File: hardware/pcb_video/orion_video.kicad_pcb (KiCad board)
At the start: 4 copper layers, 99.7 x 99.7 mm, 0 parts

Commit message: Обновлена схема видеомодуля
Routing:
- removed copper zone on In1.Cu, net GND
- removed copper zone on In2.Cu, net VCC
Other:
- copper layers 4 -> 2

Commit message: Предварительное размещение элементов
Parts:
- added C1: 0.1u, Capacitors_SMD:C_0805, B.Cu at (190.5, 29.8)
- added C10: 0.1u, Capacitors_SMD:C_0805, F.Cu at (186.7, 132.7)
- added C11: 0.1u, Capacitors_SMD:C_0805, F.Cu at (190.5, 132.7)
- added C12: 0.1u, Capacitors_SMD:C_0805, F.Cu at (194.3, 132.7)
- added C13: 0.1u, Capacitors_SMD:C_0805, F.Cu at (198.1, 132.7)
- added C14: 0.1u, Capacitors_SMD:C_0805, F.Cu at (201.9, 132.7)
- added C15: 0.1u, Capacitors_SMD:C_0805, F.Cu at (171.4, 135.9)
- added C16: 0.1u, Capacitors_SMD:C_0805, F.Cu at (175.3, 135.9)
- added C17: 0.1u, Capacitors_SMD:C_0805, F.Cu at (179.1, 135.9)
- added C18: 0.1u, Capacitors_SMD:C_0805, F.Cu at (182.9, 135.9)
- added C19: 0.1u, Capacitors_SMD:C_0805, F.Cu at (186.7, 135.9)
- added C2: 10u, Capacitors_Tantalum_SMD:CP_Tantalum_Case-B_EIA-3528-21_Hand, F.Cu at (175.9, 127.6)
- added C20: 0.1u, Capacitors_SMD:C_0805, F.Cu at (190.5, 135.9)
- added C21: 0.1u, Capacitors_SMD:C_0805, F.Cu at (194.3, 135.9)
- added C22: 0.1u, Capacitors_SMD:C_0805, F.Cu at (198.1, 135.9)
- added C23: 0.1u, Capacitors_SMD:C_0805, F.Cu at (201.9, 135.9)
- added C24: 0.1u, Capacitors_SMD:C_0805, F.Cu at (171.4, 139.1)
- added C25: 0.1u, Capacitors_SMD:C_0805, F.Cu at (175.3, 139.1)
- added C26: 0.1u, Capacitors_SMD:C_0805, F.Cu at (179.1, 139.1)
- added C27: 0.1u, Capacitors_SMD:C_0805, F.Cu at (182.9, 139.1)
- added C28: 0.1u, Capacitors_SMD:C_0805, F.Cu at (186.7, 139.1)
- added C29: 0.1u, Capacitors_SMD:C_0805, F.Cu at (190.5, 139.1)
- added C3: 10u, Capacitors_Tantalum_SMD:CP_Tantalum_Case-B_EIA-3528-21_Hand, F.Cu at (184.5, 127.6)
- added C30: 0.1u, Capacitors_SMD:C_0805, F.Cu at (194.3, 139.1)
- added C31: 0.1u, Capacitors_SMD:C_0805, F.Cu at (198.1, 139.1)
- added C4: 10u, Capacitors_Tantalum_SMD:CP_Tantalum_Case-B_EIA-3528-21_Hand, F.Cu at (192.8, 127.6)
- added C5: 10u, Capacitors_Tantalum_SMD:CP_Tantalum_Case-B_EIA-3528-21_Hand, F.Cu at (201.1, 127.6)
- added C6: 0.1u, Capacitors_SMD:C_0805, F.Cu at (171.4, 132.7)
- added C7: 0.1u, Capacitors_SMD:C_0805, F.Cu at (175.3, 132.7)
- added C8: 0.1u, Capacitors_SMD:C_0805, F.Cu at (179.1, 132.7)
- added C9: 0.1u, Capacitors_SMD:C_0805, F.Cu at (182.9, 132.7)
- added DD1: IE18, Housings_SOIC:SOIC-16_3.9x9.9mm_Pitch1.27mm, F.Cu at (155.6, 64.1)
- added DD10: IR35, Housings_SOIC:SOIC-20W_7.5x12.8mm_Pitch1.27mm, F.Cu at (186.1, 104.1)
- added DD11: IR23, Housings_SOIC:SOIC-20W_7.5x12.8mm_Pitch1.27mm, F.Cu at (186.1, 89.5)
- added DD12: IR22, Housings_SOIC:SOIC-20W_7.5x12.8mm_Pitch1.27mm, F.Cu at (109.2, 61.6)
- added DD13: IR22, Housings_SOIC:SOIC-20W_7.5x12.8mm_Pitch1.27mm, F.Cu at (108.6, 76.2)
- added DD14: IR22, Housings_SOIC:SOIC-20W_7.5x12.8mm_Pitch1.27mm, F.Cu at (123.8, 76.2)
- added DD15: IR22, Housings_SOIC:SOIC-20W_7.5x12.8mm_Pitch1.27mm, B.Cu at (108.6, 76.2)
- added DD16: IR22, Housings_SOIC:SOIC-20W_7.5x12.8mm_Pitch1.27mm, B.Cu at (123.8, 76.2)
- added DD17: KP11, Housings_SOIC:SOIC-16_3.9x9.9mm_Pitch1.27mm, F.Cu at (125.7, 62.2)
- added DD18: 28C256, Sockets:PLCC44, F.Cu at (120.0, 42.5)
- added DD19: IR10, Housings_SOIC:SOIC-16_3.9x9.9mm_Pitch1.27mm, F.Cu at (141.6, 34.9)
- added DD2: IE18, Housings_SOIC:SOIC-16_3.9x9.9mm_Pitch1.27mm, F.Cu at (146.1, 64.1)
- added DD20: IR10, Housings_SOIC:SOIC-16_3.9x9.9mm_Pitch1.27mm, F.Cu at (155.6, 34.9)
- added DD21: IR10, Housings_SOIC:SOIC-16_3.9x9.9mm_Pitch1.27mm, F.Cu at (141.6, 47.6)
- added DD22: IR10, Housings_SOIC:SOIC-16_3.9x9.9mm_Pitch1.27mm, F.Cu at (155.6, 47.6)
- added DD23: ATF22V10, Housings_DIP:DIP-24_W7.62mm_Socket_LongPads, F.Cu at (167.6, 52.7)
- added DD24: KP11, Housings_SOIC:SOIC-16_3.9x9.9mm_Pitch1.27mm, F.Cu at (158.8, 87.6)
- added DD25: KP11, Housings_SOIC:SOIC-16_3.9x9.9mm_Pitch1.27mm, B.Cu at (158.8, 91.4)
- added DD26: KP11, Housings_SOIC:SOIC-16_3.9x9.9mm_Pitch1.27mm, F.Cu at (158.8, 97.2)
- added DD27: KP11, Housings_SOIC:SOIC-16_3.9x9.9mm_Pitch1.27mm, B.Cu at (158.8, 101.0)
- added DD28: ATF22V10, Housings_DIP:DIP-24_W7.62mm_Socket_LongPads, F.Cu at (139.7, 88.3)
- added DD29: AP6, Housings_SOIC:SOIC-20W_7.5x12.8mm_Pitch1.27mm, F.Cu at (120.0, 106.0)
- added DD3: IE18, Housings_SOIC:SOIC-16_3.9x9.9mm_Pitch1.27mm, F.Cu at (136.5, 64.1)
- added DD30: AP6, Housings_SOIC:SOIC-20W_7.5x12.8mm_Pitch1.27mm, B.Cu at (120.0, 106.0)
- added DD31, DD32: CY7C1049B, andreil:SOJ-36, F.Cu at (148.9, 132.0)
- added DD4: IE18, Housings_SOIC:SOIC-16_3.9x9.9mm_Pitch1.27mm, F.Cu at (174.6, 64.1)
- added DD5: IE18, Housings_SOIC:SOIC-16_3.9x9.9mm_Pitch1.27mm, F.Cu at (184.2, 64.1)
- added DD6: IE18, Housings_SOIC:SOIC-16_3.9x9.9mm_Pitch1.27mm, F.Cu at (193.7, 64.1)
- added DD7: ATF22V10, Housings_DIP:DIP-24_W7.62mm_Socket_LongPads, F.Cu at (161.9, 73.0)
- added DD8: ATF22V10, Housings_DIP:DIP-24_W7.62mm_Socket_LongPads, F.Cu at (195.6, 73.0)
- added DD9: IR35, Housings_SOIC:SOIC-20W_7.5x12.8mm_Pitch1.27mm, F.Cu at (136.5, 106.0)
- added J1: VGA, w_conn_pc:DB_15F-VGA, F.Cu at (182.0, 23.6)
- added J2: SYS_PRO, Socket_Strips:Socket_Strip_Straight_2x32_Pitch2.54mm, F.Cu at (109.9, 114.9)
- added J3: SYS_EXT, Socket_Strips:Socket_Strip_Straight_2x18_Pitch2.54mm, F.Cu at (109.2, 25.4)
- added J4: MEM1, Socket_Strips:Socket_Strip_Straight_2x12_Pitch2.00mm, F.Cu at (149.3, 85.9)
- added J5: MEM2, Socket_Strips:Socket_Strip_Straight_2x12_Pitch2.00mm, F.Cu at (105.4, 85.9)
- added JP1: 4:3, Socket_Strips:Socket_Strip_Straight_1x02_Pitch2.54mm, F.Cu at (169.5, 85.1)
- added JP2: GDS, Socket_Strips:Socket_Strip_Straight_2x08_Pitch2.54mm, F.Cu at (105.4, 34.3)
- added R1: 1k, Resistors_SMD:R_0805, F.Cu at (156.2, 128.9)
- added R10: 470, Resistors_SMD:R_0805, F.Cu at (177.8, 34.9)
- added R11: 470, Resistors_SMD:R_0805, F.Cu at (181.6, 40.0)
- added R12: 470, Resistors_SMD:R_0805, F.Cu at (181.6, 34.9)
- added R13: 1k, Resistors_SMD:R_0805, F.Cu at (175.3, 37.5)
- added R14: 1k, Resistors_SMD:R_0805, F.Cu at (179.1, 37.5)
- added R15: 1k, Resistors_SMD:R_0805, F.Cu at (182.9, 37.5)
- added R16: 510, Resistors_SMD:R_0805, F.Cu at (175.9, 33.7)
- added R17: 510, Resistors_SMD:R_0805, F.Cu at (179.7, 33.7)
- added R18: 510, Resistors_SMD:R_0805, F.Cu at (183.5, 33.7)
- added R19: 47, Resistors_SMD:R_0805, B.Cu at (181.6, 33.7)
- added R2: 1k, Resistors_SMD:R_0805, F.Cu at (159.4, 128.9)
- added R20: 47, Resistors_SMD:R_0805, B.Cu at (185.4, 33.7)
- added R3: 1k, Resistors_SMD:R_0805, F.Cu at (162.6, 128.9)
- added R4: 1k, Resistors_SMD:R_0805, F.Cu at (165.7, 128.9)
- added R5: 1k, Resistors_SMD:R_0805, F.Cu at (156.2, 132.0)
- added R6: 1k, Resistors_SMD:R_0805, F.Cu at (159.4, 132.1)
- added R7: 470, Resistors_SMD:R_0805, F.Cu at (174.0, 40.0)
- added R8: 470, Resistors_SMD:R_0805, F.Cu at (174.0, 34.9)
- added R9: 470, Resistors_SMD:R_0805, F.Cu at (177.8, 40.0)
- added REF**: MountingHole_3.2mm_M3_Pad, Mounting_Holes:MountingHole_3.2mm_M3_Pad, F.Cu at (194.3, 116.2)
- added REF**: MountingHole_3.2mm_M3_Pad, Mounting_Holes:MountingHole_3.2mm_M3_Pad, F.Cu at (103.5, 116.2)
- added REF**: MountingHole_3.2mm_M3_Pad, Mounting_Holes:MountingHole_3.2mm_M3_Pad, F.Cu at (103.5, 27.3)
- added REF**: MountingHole_3.2mm_M3_Pad, Mounting_Holes:MountingHole_3.2mm_M3_Pad, F.Cu at (193.7, 36.8)
- added U1, U2: AS7C4098A, andreil:SOJ-44, F.Cu at (148.9, 132.0)
- added Y1: 25MHz, Crystals:Crystal_SMD_7050-4pin_7.0x5.0mm, F.Cu at (165.1, 65.4)

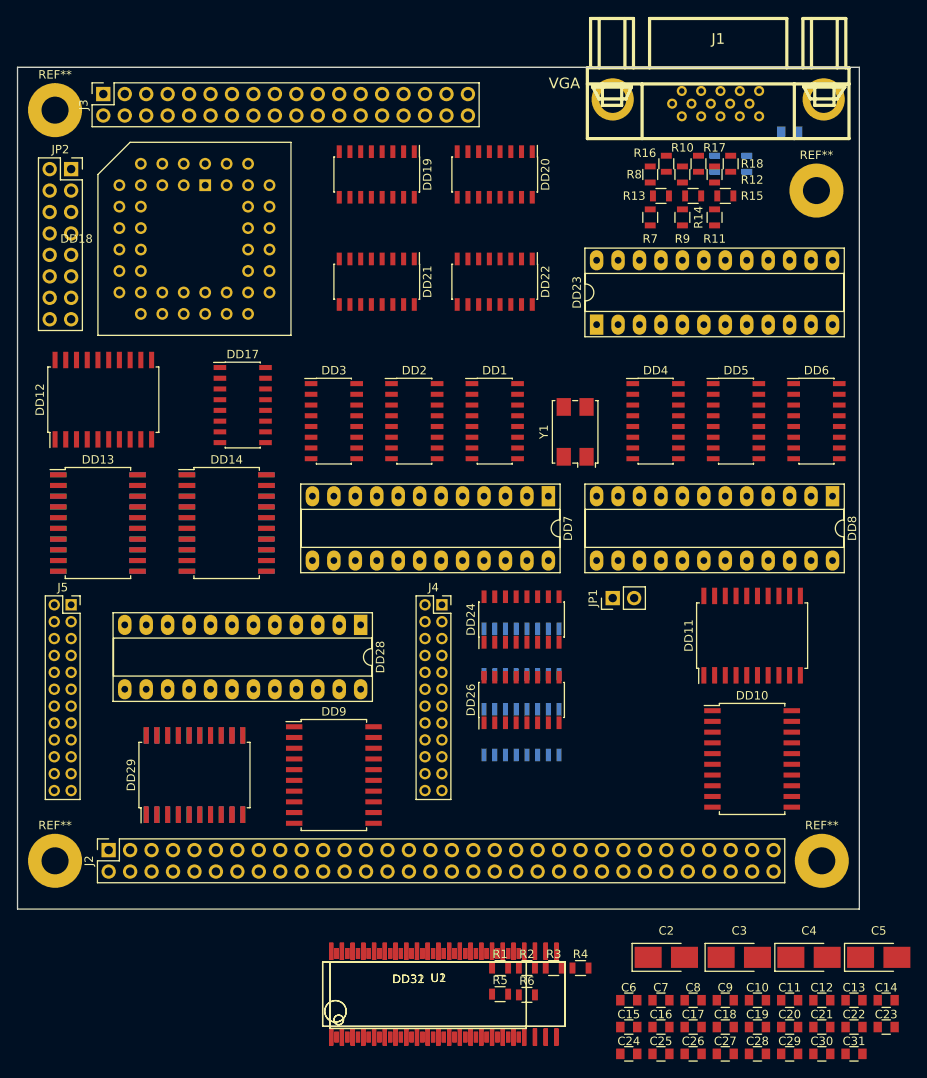
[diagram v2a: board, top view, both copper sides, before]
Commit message: Исправления по схеме видеомодуля:
1) Заменён системный разъём на DIN 41612;
2) ПЗУ знакогенератора заменена на 28C512;
3) Добавлена коммутация подачи питания на пин 9 разъёма VGA.
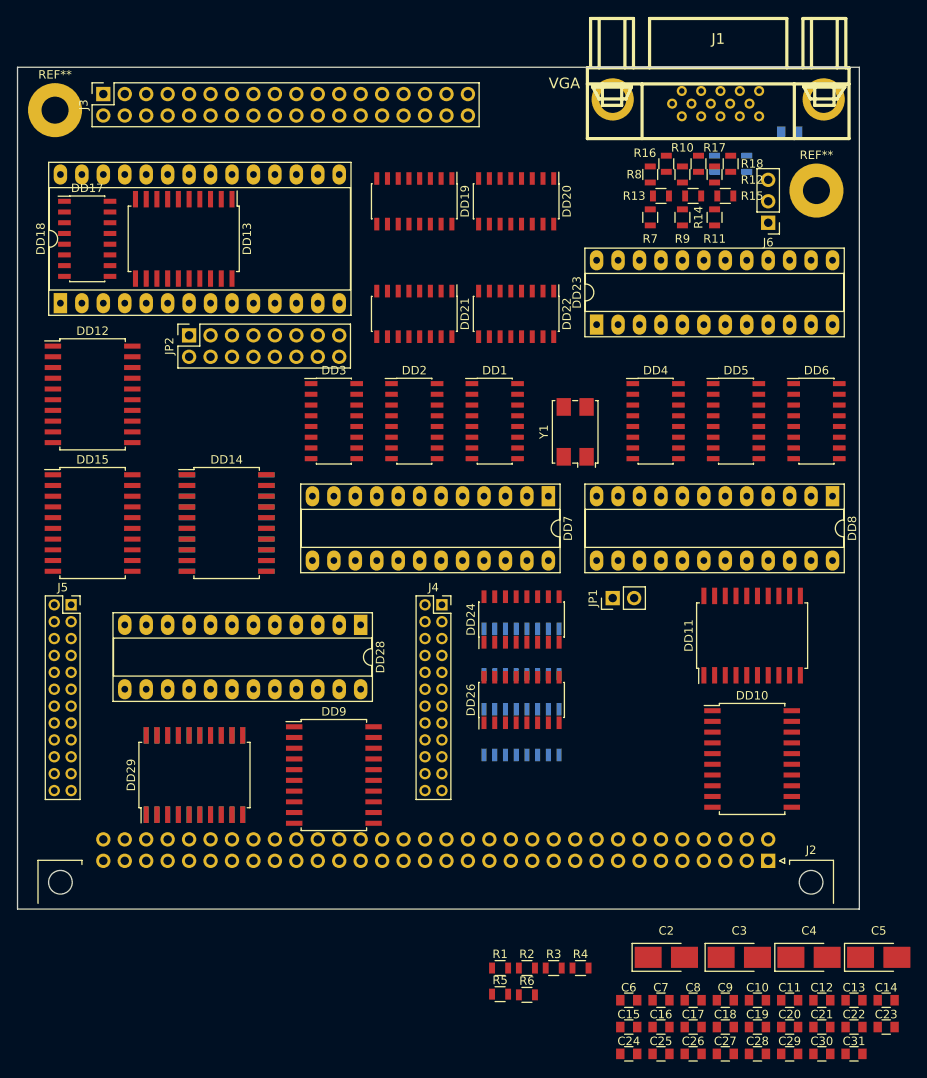
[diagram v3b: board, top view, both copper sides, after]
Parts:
- removed DD31, DD32: CY7C1049B, andreil:SOJ-36
- removed the REF** at (194.3, 116.2)
- removed the REF** at (103.5, 116.2)
- removed U1, U2: AS7C4098A, andreil:SOJ-44
- added J6: VGAP, Socket_Strips:Socket_Strip_Straight_1x03_Pitch2.54mm, F.Cu at (188.0, 40.6)
- DD15: moved to F.Cu
- DD18: value 28C256 -> 28C512; footprint Sockets:PLCC44 -> Housings_DIP:DIP-28_W15.24mm_Socket_LongPads
- J2: footprint Socket_Strips:Socket_Strip_Straight_2x32_Pitch2.54mm -> orion:DIN41612_B064M
- moved J2 78.1 mm to (188.0, 116.2), turned to 180 degrees
- moved DD13 35.2 mm to (118.7, 42.5), turned to 270 degrees
- moved DD17 27.0 mm to (107.3, 42.5)
- moved JP2 24.1 mm to (119.4, 54.0), turned to 90 degrees
- moved DD18 17.6 mm to (104.1, 50.2), turned to 90 degrees
- moved DD21 5.85 mm to (146.1, 51.4)
- moved DD19 5.46 mm to (146.1, 38.1)
- moved DD22 4.58 mm to (158.1, 51.4)
- moved DD20 4.07 mm to (158.1, 38.1)
- moved DD12 1.42 mm to (108.0, 61.0), turned to 0 degrees
- moved DD15 0.63 mm to (108.0, 76.2), turned to 0 degrees
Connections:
- DD18 pad 1: /F3 -> /PGD
- DD18 pad 27: GND -> /F3
- J1 pad 9: VCC -> Net-(J1-Pad9)

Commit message: Исправлен системный разъём - выполнен 3-х рядным DIN
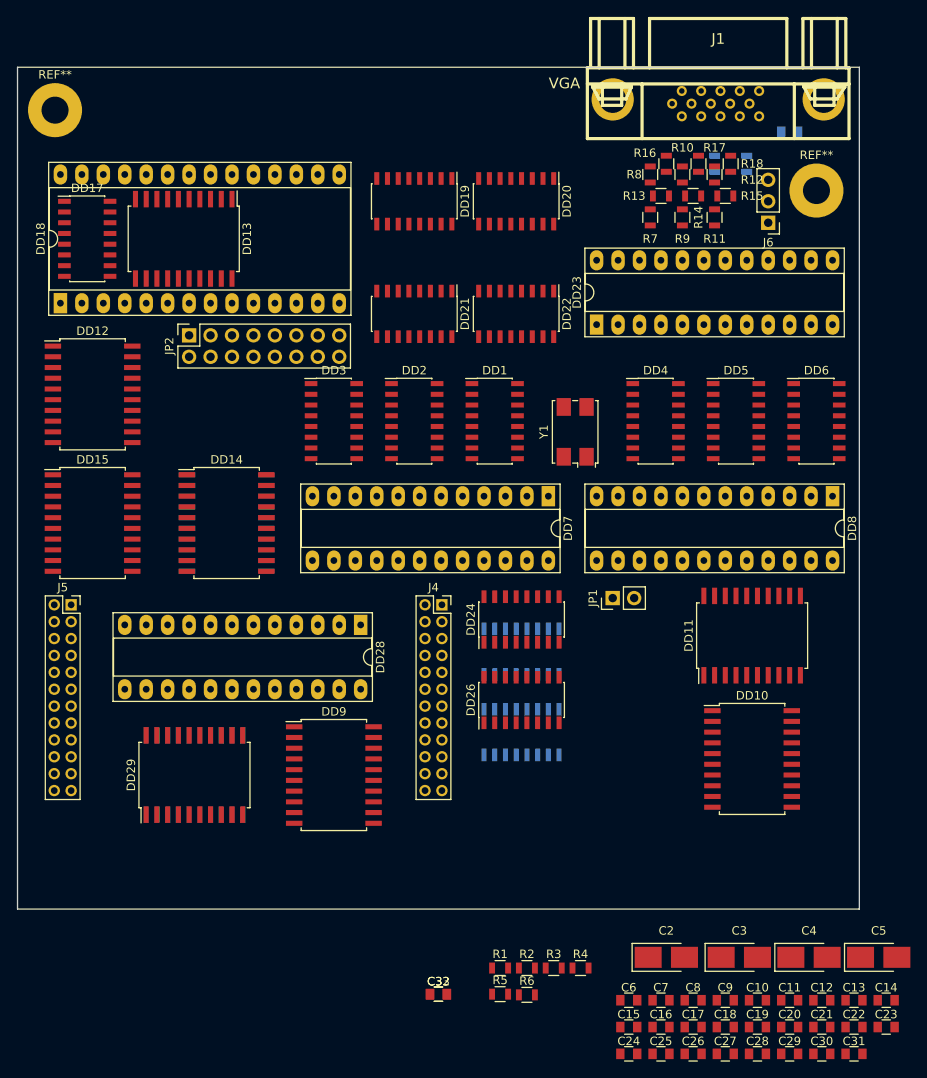
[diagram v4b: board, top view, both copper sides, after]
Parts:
- removed J2: SYS_PRO, orion:DIN41612_B064M
- removed J3: SYS_EXT, Socket_Strips:Socket_Strip_Straight_2x18_Pitch2.54mm
- added C32, C33: 0.1u, Capacitors_SMD:C_0805, F.Cu at (148.9, 132.0)

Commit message: Обновлено расположение компонентов, разъём SYSTEM заменён на 3-х рядный.
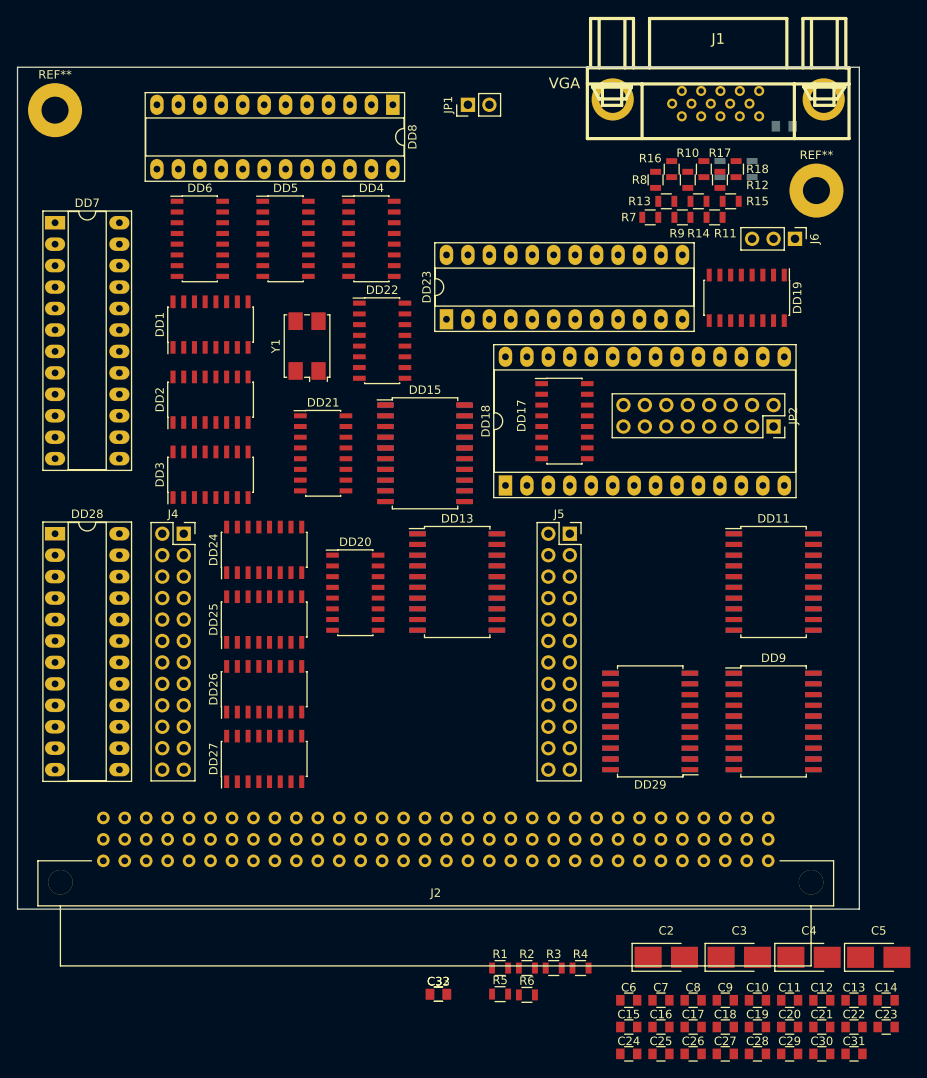
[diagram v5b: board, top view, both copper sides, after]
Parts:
- added J2: SYSTEM, Connectors_IEC_DIN:Socket_DIN41612-CaseC1-full-Male-96Pin-3rows, F.Cu at (148.6, 113.7)
- DD10, DD12, DD14: moved to B.Cu
- DD25, DD27: moved to F.Cu
- J4, J5: footprint Socket_Strips:Socket_Strip_Straight_2x12_Pitch2.00mm -> Socket_Strips:Socket_Strip_Straight_2x12_Pitch2.54mm
- moved DD12 83.7 mm to (188.6, 83.2)
- moved DD6 76.1 mm to (120.7, 42.5)
- moved JP2 70.1 mm to (188.6, 64.8), turned to 270 degrees
- moved DD8 69.7 mm to (143.5, 26.7)
- moved DD7 66.8 mm to (103.5, 40.6), turned to 0 degrees
- moved JP1 60.9 mm to (152.4, 26.7)
- moved DD17 60.5 mm to (163.8, 64.1)
- moved J5 59.7 mm to (164.5, 77.5)
- moved DD5 57.5 mm to (130.8, 42.5)
- moved DD18 57.0 mm to (156.8, 71.8)
- moved DD29 54.3 mm to (174.0, 99.7), turned to 180 degrees
- moved DD30 54.3 mm to (174.0, 99.7), turned to 180 degrees
- moved DD9 52.5 mm to (188.6, 99.7)
- moved DD13 52.0 mm to (151.1, 83.2), turned to 0 degrees
- moved DD20 50.1 mm to (139.1, 84.5), turned to 0 degrees
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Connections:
- J5 pad 10: /MD7 -> /MD8
- J5 pad 11: /MD8 -> /MD1
- J5 pad 13: /MD10 -> /MD2
- J5 pad 14: /MD11 -> /MD10
- J5 pad 15: /MD12 -> /MD3
- J5 pad 16: /MD13 -> /MD11
- J5 pad 17: /MD14 -> /MD4
- J5 pad 18: /MD15 -> /MD12
- J5 pad 19: /OE -> /MD5
- J5 pad 20: /WE -> /MD13
- J5 pad 21: /SU -> /MD6
- J5 pad 22: /SL -> /MD14
- J5 pad 23: /CE0 -> /MD7
- J5 pad 24: /CE1 -> /MD15
- J5 pad 3: /MD0 -> /OE
- J5 pad 4: /MD1 -> /WE
- J5 pad 5: /MD2 -> /SU
- J5 pad 6: /MD3 -> /SL
- J5 pad 7: /MD4 -> /CE0
- J5 pad 8: /MD5 -> /CE1
- J5 pad 9: /MD6 -> /MD0
